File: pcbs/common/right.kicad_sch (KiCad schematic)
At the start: 89 parts, among them J2 TRS

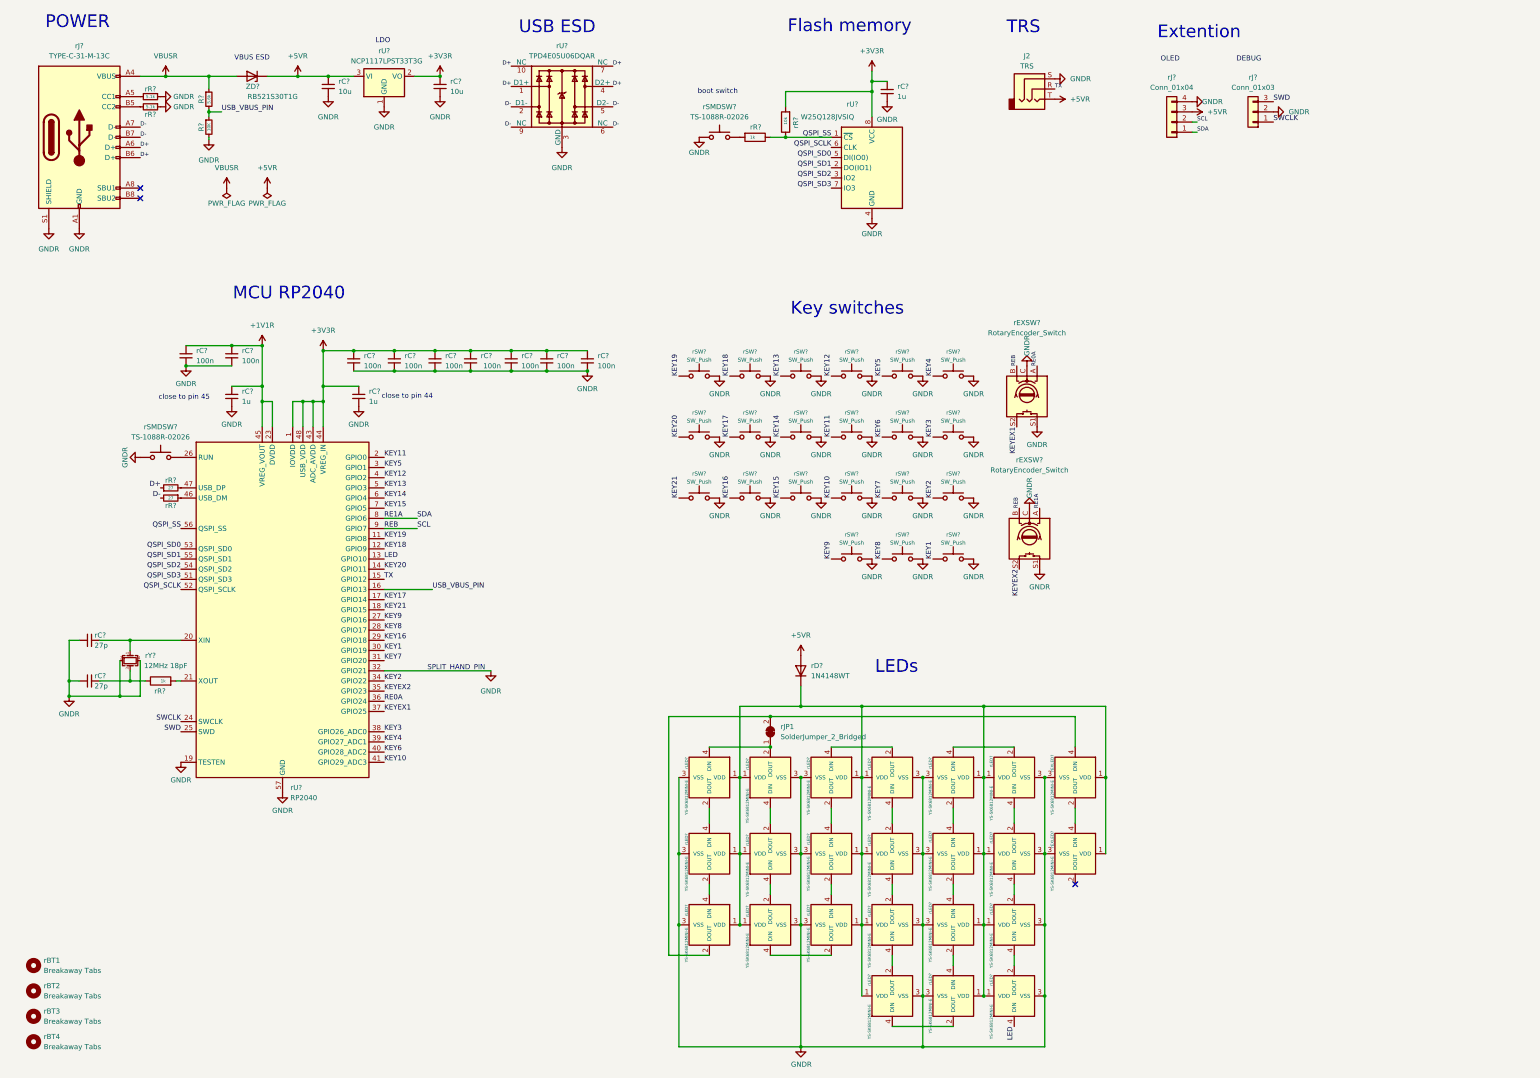
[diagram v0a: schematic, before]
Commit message: PCB re-route for EMI (cherry)
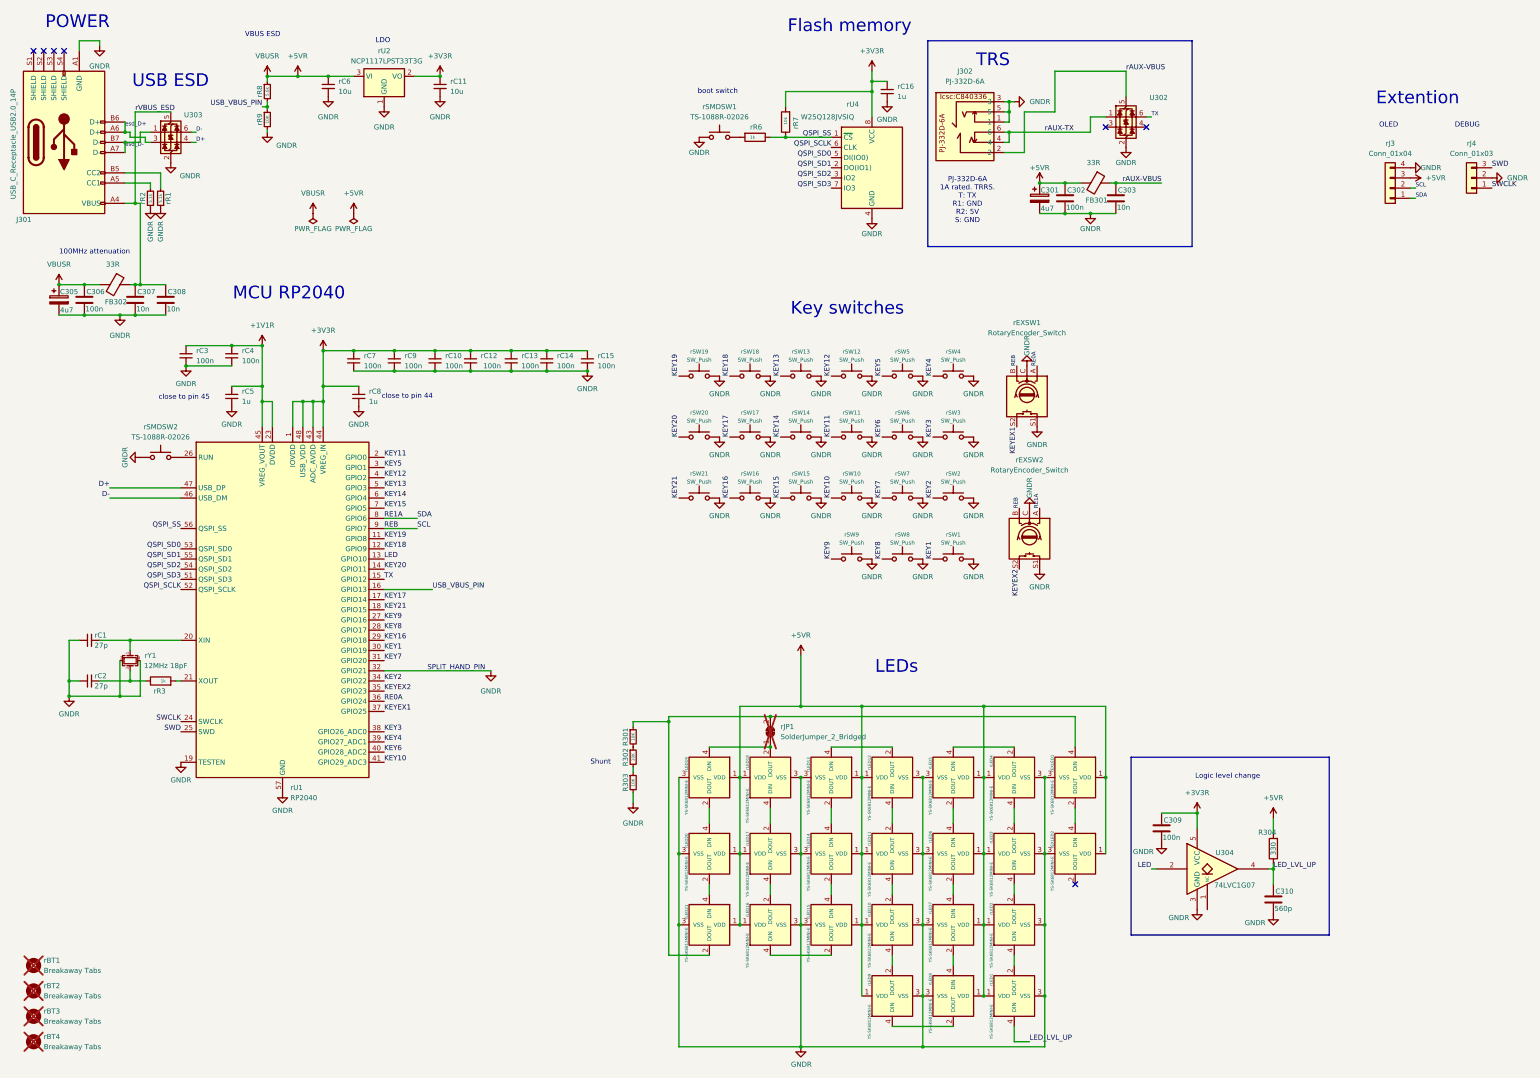
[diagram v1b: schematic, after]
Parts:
- removed J2: TRS, kbd_local:PJ-398A-5A_PJ-399B-6A, symbol Connector_Audio:AudioJack3
- removed ZD?: RB521S30T1G, Diode_SMD:D_SOD-523, symbol Diode:ESD5Zxx
- removed rD?: 1N4148WT, Diode_SMD:D_SOD-523, symbol Diode:1N4148WT
- removed rJ?: TYPE-C-31-M-13C, kbd_local:TYPE-C-31-M-13C, symbol Connector:USB_C_Receptacle_USB2.0
- removed rR? (x2): 27, Resistor_SMD:R_0402_1005Metric, symbol Device:R_Small
- removed rU?: TPD4E05U06DQAR, Package_SON:USON-10_2.5x1.0mm_P0.5mm, symbol Power_Protection:TPD4EUSB30
- added C301, C305: 4u7, Capacitor_SMD:C_1210_3225Metric, symbol Device:C_Polarized
- added C302, C306, C309: 100n, Capacitor_SMD:C_0402_1005Metric, symbol Device:C
- added C303, C307, C308: 10n, Capacitor_SMD:C_0402_1005Metric, symbol Device:C
- added C310: 560p, Capacitor_SMD:C_0402_1005Metric, symbol Device:C
- added FB301, FB302: 33R, Inductor_SMD:L_1206_3216Metric, symbol Device:FerriteBead
- added J301: USB_C_Receptacle_USB2.0_14P, keyboard_ohne_emi:USB4105, symbol Connector:USB_C_Receptacle_USB2.0_14P
- added J302: PJ-332D-6A, keyboard_ohne_emi:PJ-332D-6A, symbol kbd:TRRS_1A
- added R301, R302, R303: 10K, Resistor_SMD:R_0402_1005Metric, symbol Device:R_Small
- added R304: 330, Resistor_SMD:R_0402_1005Metric, symbol Device:R
- added U302, U303: USBLC6-2P6, ESP32-S3-CaV2:USBLC6-2P6, symbol Power_Protection:USBLC6-2P6
- added U304: 74LVC1G07, Package_TO_SOT_SMD:SOT-353_SC-70-5, symbol 74xGxx:74LVC1G07
- rBT1, rBT2, rBT3, rBT4, rJP1: now not fitted
- rC10, rC12, rC13, rC14, rC15, rC3, rC4, rC7, rC9: renamed from rC?; JLCPCB Part # (none) -> C133086; LCSC Part # (none) -> C133086
- rSMDSW1, rSMDSW2: renamed from rSMDSW?; LCSC Part # (none) -> C455280
- rU1: renamed from rU?; LCSC Part # (none) -> C2040
- rU2: renamed from rU?; LCSC Part # (none) -> C146799
- rU4: renamed from rU?; LCSC Part # (none) -> C113767
- rY1: renamed from rY?; LCSC Part # (none) -> C91749
- gave numbers to parts that had none: 62
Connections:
- net VBUSR is gone; now on net +5VR: rR8.1
- net +3V3R: now also C309.1, U304.5 (VCC)
- net +5VR: now also rEXLED1.1 (VDD), rEXLED2.1 (VDD), rLED1.1 (VDD), rLED10.1 (VDD), rLED11.1 (VDD), rLED12.1 (VDD), rLED13.1 (VDD), rLED14.1 (VDD), rLED15.1 (VDD), rLED16.1 (VDD), rLED17.1 (VDD), rLED18.1 (VDD), rLED19.1 (VDD), rLED2.1 (VDD), rLED20.1 (VDD), rLED21.1 (VDD), rLED3.1 (VDD), rLED4.1 (VDD), rLED5.1 (VDD), rLED6.1 (VDD), rLED7.1 (VDD), rLED8.1 (VDD), rLED9.1 (VDD), C301.1, C302.1, C305.1, C306.1, FB301.2, FB302.2, R304.2
- net D+: now also rU1.47 (USB_DP), U303.4 (I/O2)
- net D-: now also rU1.46 (USB_DM), U303.6 (I/O1)
- net GNDR: now also C301.2, C302.2, C303.2, C305.2, C306.2, C307.2, C308.2, C309.2, C310.2, J301.A1 (GND), J301.B1 (GND), J302.1, J302.3, J302.5, R303.2, U302.2 (GND), U303.2 (GND), U304.3 (GND)
- net LED: now also U304.2; no longer rLED1.4 (DIN)
- net TX: now also U302.6 (I/O1)
- net at rR1.2: now also J301.B5 (CC2)
- net at rR2.2: now also J301.A5 (CC1)
- net at rEXLED1.4 (DIN), rJP1.2 (B), rLED21.2 (DOUT): now also R301.1
- new net: R302.2, R303.1
- new net: R301.2, R302.1
- new net LED_LVL_UP: C310.1, R304.1, U304.4, rLED1.4 (DIN)
- new net esd_D+: J301.A6 (D+), J301.B6 (D+), U303.3 (I/O2)
- new net esd_D-: J301.A7 (D-), J301.B7 (D-), U303.1 (I/O1)
- new net rAUX-TX: J302.4, J302.6, U302.1 (I/O1)
- new net rAUX-VBUS: C303.1, FB301.1, J302.2, U302.5 (VBUS)
- new net rVBUS_ESD: C307.1, C308.1, FB302.1, J301.A4 (VBUS), J301.B4 (VBUS), U303.5 (VBUS)
- no-connect marks 3 -> 7
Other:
- note added: "100MHz attenuation"
- note added: "Logic level change"
- note added: "PJ-332D-6A 1A rated. TRRS. T: TX R1: GND R2: 5V S: GND"
- note added: "Shunt"
- moved on the sheet: rJ3, rJ4, rR1, rR2, rR8, rR9
